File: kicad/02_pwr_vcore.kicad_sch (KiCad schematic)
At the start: 7 parts, among them U201 TLV62585PDRLR

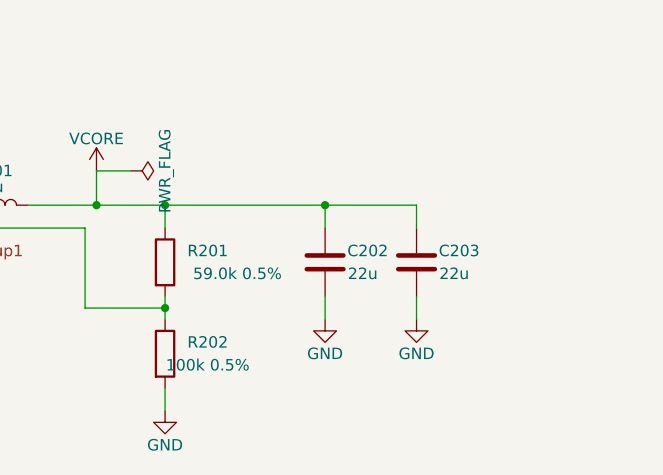
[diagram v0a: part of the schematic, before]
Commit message: Phase 3 (half): checklist fixes in the schematic; board placement still to do
- R801 240R 0.1 % (RT0402BRD07240RL, C852660); SSU_N (L4) 10 k pull-up R622 to 1V8.
- Efinix decoupling table in full on sheet 05 (now A2): C5001-C5073 (0201 10n/1n/100n,
  0402 1u/4u7, 0805 10u/47u, 1206 100u).
- Each TLV62585 cell: 47u output cap and a 22p feed-forward cap across R1 (data sheet:
  feed-forward needed above 47 uF; user decision).
- build_schematic.sh fails on duplicate references (ERC misses them).
- tools/add_parts.py: add missing schematic parts to a routed board; tools/place_free.py
  (untested): nearest free B.Cu spot.
- kicad/ti135_card.kicad_pcb unchanged; placement in work/p3, see NEXT_SESSION.md.

Co-Authored-By: Claude Opus 5.5 <noreply@anthropic.com>
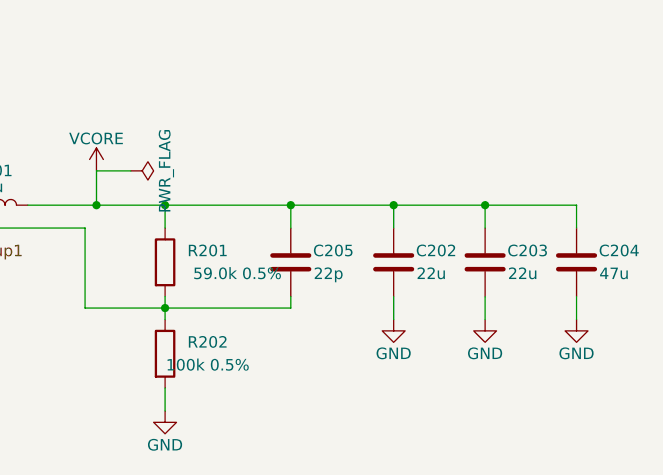
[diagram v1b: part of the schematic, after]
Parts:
- added C204: 47u, Capacitor_SMD:C_0805_2012Metric, symbol ti135_card:C
- added C205: 22p, Capacitor_SMD:C_0402_1005Metric, symbol ti135_card:C
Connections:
- net GND: now also C204.2
- net VCORE: now also C204.1, C205.1
- net at R201.2, R202.1, U201.5 (FB): now also C205.2
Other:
- moved on the sheet: C202, C203

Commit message: LCSC numbers for all JLC parts; Y701 -> YXC OT322525MJBA4SL
- tools/set_lcsc.py: one table (value, footprint) -> LCSC, fills empty LCSC fields in the
  sheets; 312 symbols. JLC basic parts where available, cap voltages checked per rail,
  VCORE divider 0.1 % (no 0.5 % in stock). Board fields synced with add_parts.py.
- Y701: the SiT8924 has no JLC stock; now YXC OT322525MJBA4SL (C669088, 3225), EN tied
  to 1V8. R701/C701 moved 0.5 mm to clear its courtyard. Netlist change: Y701 pin 1 -> 1V8.
- Only U501 (Ti135) is left without LCSC (global sourcing / consigned).
- DRC: schematic parity 0.

Co-Authored-By: Claude Opus 5.5 <noreply@anthropic.com>
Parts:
- C201: LCSC (none) -> C15850
- C202, C203: LCSC (none) -> C45783
- C204: LCSC (none) -> C16780
- C205: LCSC (none) -> C1555
- R201: LCSC (none) -> C2684527
- R202: LCSC (none) -> C136979
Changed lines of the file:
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@@
+			)
+		)
+		(property "LCSC" "C45783"
+			(at 142.24 67.31 0)
+			(effects
+				(font
+					(size 1.27 1.27)
+				)
+				(hide yes)
 			)
 		)
@@
 			)
 		)
+		(property "LCSC" "C1555"
+			(at 130.81 67.31 0)
+			(effects
+				(font
+					(size 1.27 1.27)
+				)
+				(hide yes)
+			)
+		)
 		(pin "1"
 		)
@@
 			)
 		)
+		(property "LCSC" "C15850"
+			(at 50.8 67.31 0)
+			(effects
+				(font
+					(size 1.27 1.27)
+				)
+				(hide yes)
+			)
+		)
 		(pin "1"
 		)
@@
 			)
 		)
+		(property "LCSC" "C16780"
+			(at 162.56 67.31 0)
+			(effects
+				(font
+					(size 1.27 1.27)
+				)
+				(hide yes)
+			)
+		)
 		(pin "1"
 		)
@@
 			)
 		)
+		(property "LCSC" "C136979"
+			(at 116.84 77.47 0)
+			(effects
+				(font
+					(size 1.27 1.27)
+				)
+				(hide yes)
+			)
+		)
 		(pin "1"
 		)
@@
 			)
 		)
+		(property "LCSC" "C2684527"
+			(at 116.84 67.31 0)
+			(effects
+				(font
+					(size 1.27 1.27)
+				)
+				(hide yes)
+			)
+		)
 		(pin "1"
 		)
@@
 			)
 		)
+		(property "LCSC" "C45783"
+			(at 152.4 67.31 0)
+			(effects
+				(font
+					(size 1.27 1.27)
+				)
+				(hide yes)
+			)
+		)
